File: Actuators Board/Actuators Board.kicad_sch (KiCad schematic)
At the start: 73 parts, among them J1 Conn_01x05_Male, J10 Conn_01x02_Male, J2 Solenoid(Sol), J4 Conn_01x03_Male, J5 Conn_01x06_Male, J9 Conn_01x02_Male, Q1 MMDT2222A, Q2 SI2366DS, U1 ESP32-PICO-D4, U2 TPS54233D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

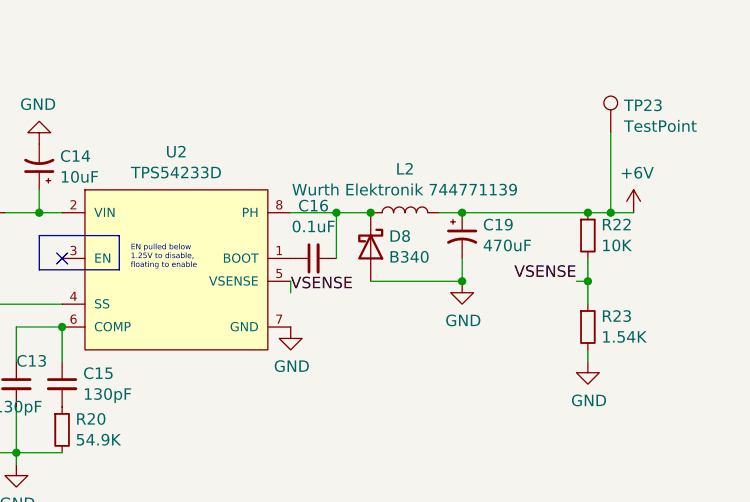
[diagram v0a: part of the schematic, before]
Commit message: Preliminary layout of buck converter components
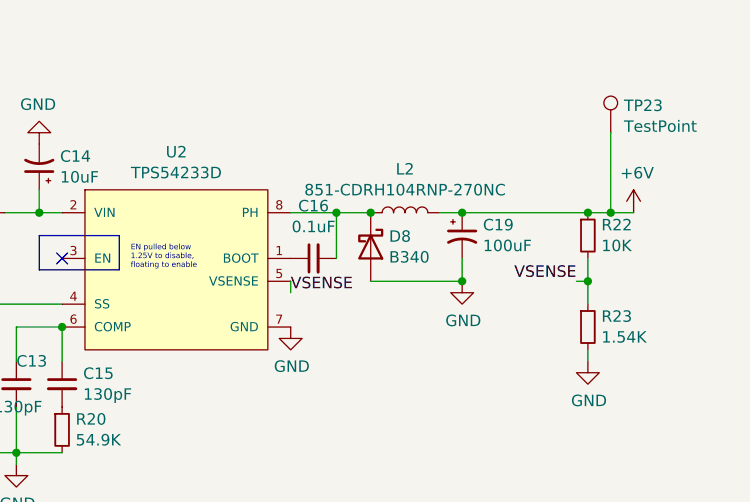
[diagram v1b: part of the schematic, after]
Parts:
- C14: footprint Capacitor_SMD:C_0603_1608Metric -> Capacitor_SMD:CP_Elec_3x5.3
- C19: value 470uF -> 100uF; footprint Capacitor_SMD:CP_Elec_6.3x7.7 -> Capacitor_SMD:CP_Elec_5x5.9
- L2: value Wurth Elektronik 744771139 -> 851-CDRH104RNP-270NC; footprint Inductor_SMD:L_12x12mm_H6mm -> Inductor_SMD:L_10.4x10.4_H4.8
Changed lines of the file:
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@@
     (in_bom yes) (on_board yes)
     (property "Reference" "L2" (id 0) (at 248.92 29.464 90))
-    (property "Value" "Wurth Elektronik 744771139 " (id 1) (at 248.92 31.7754 90))
-    (property "Footprint" "Inductor_SMD:L_12x12mm_H6mm" (id 2) (at 248.92 34.29 0)
+    (property "Value" "851-CDRH104RNP-270NC" (id 1) (at 248.92 31.7754 90))
+    (property "Footprint" "Inductor_SMD:L_10.4x10.4_H4.8" (id 2) (at 248.92 34.29 0)
       (effects (font (size 1.27 1.27)) hide)
     )
@@
     (pin "2")
   )
-  (symbol (lib_id "Connector:TestPoint") (at 34.29 74.93 270)
+  (symbol (lib_id "Connector:TestPoint") (at 34.29 74.93 270) (unit 1)
     (in_bom yes) (on_board yes)
     (property "Reference" "TP4" (id 0) (at 39.0652 73.7616 90)
@@
     (pin "1")
   )
-  (symbol (lib_id "Connector:TestPoint") (at 34.29 72.39 270)
+  (symbol (lib_id "Connector:TestPoint") (at 34.29 72.39 270) (unit 1)
     (in_bom yes) (on_board yes)
     (property "Reference" "TP3" (id 0) (at 39.0652 71.2216 90)
@@
     (pin "1")
   )
-  (symbol (lib_id "Connector:TestPoint") (at 34.29 69.85 270)
+  (symbol (lib_id "Connector:TestPoint") (at 34.29 69.85 270) (unit 1)
     (in_bom yes) (on_board yes)
     (property "Reference" "TP2" (id 0) (at 39.0652 68.6816 90)
@@
     (pin "1")
   )
-  (symbol (lib_id "Connector:TestPoint") (at 34.29 67.31 270)
+  (symbol (lib_id "Connector:TestPoint") (at 34.29 67.31 270) (unit 1)
     (in_bom yes) (on_board yes)
     (property "Reference" "TP1" (id 0) (at 39.0652 66.1416 90)
@@
       (effects (font (size 1.27 1.27)) (justify left))
     )
-    (property "Value" "470uF" (id 1) (at 257.5814 37.973 0)
-      (effects (font (size 1.27 1.27)) (justify left))
-    )
-    (property "Footprint" "Capacitor_SMD:CP_Elec_6.3x7.7" (id 2) (at 255.27 36.83 0)
+    (property "Value" "100uF" (id 1) (at 257.5814 37.973 0)
+      (effects (font (size 1.27 1.27)) (justify left))
+    )
+    (property "Footprint" "Capacitor_SMD:CP_Elec_5x5.9" (id 2) (at 255.27 36.83 0)
       (effects (font (size 1.27 1.27)) hide)
     )
@@
       (effects (font (size 1.27 1.27)) (justify right))
     )
-    (property "Footprint" "Capacitor_SMD:C_0603_1608Metric" (id 2) (at 208.28 29.21 0)
+    (property "Footprint" "Capacitor_SMD:CP_Elec_3x5.3" (id 2) (at 208.28 29.21 0)
       (effects (font (size 1.27 1.27)) hide)
     )
@@
     (pin "1")
   )
-  (symbol (lib_id "power:+3.3V") (at 58.42 92.71 270)
+  (symbol (lib_id "power:+3.3V") (at 58.42 92.71 270) (unit 1)
     (in_bom yes) (on_board yes)
     (property "Reference" "#PWR0108" (id 0) (at 54.61 92.71 0)
@@
     (pin "2")
   )
-  (symbol (lib_id "power:+3.3V") (at 97.79 46.99 0)
+  (symbol (lib_id "power:+3.3V") (at 97.79 46.99 0) (unit 1)
     (in_bom yes) (on_board yes)
     (property "Reference" "#PWR0110" (id 0) (at 97.79 50.8 0)
@@
     (pin "1")
   )
-  (symbol (lib_id "Device:C_Small") (at 95.25 49.53 180)
+  (symbol (lib_id "Device:C_Small") (at 95.25 49.53 180) (unit 1)
     (in_bom yes) (on_board yes)
     (property "Reference" "C4" (id 0) (at 92.71 50.8 0)
@@
     (pin "2")
   )
-  (symbol (lib_id "Device:C_Small") (at 100.33 49.53 0)
+  (symbol (lib_id "Device:C_Small") (at 100.33 49.53 0) (unit 1)
     (in_bom yes) (on_board yes)
     (property "Reference" "C5" (id 0) (at 102.6668 48.3616 0)
@@
     (pin "2")
   )
-  (symbol (lib_id "power:GND") (at 97.79 52.07 0)
+  (symbol (lib_id "power:GND") (at 97.79 52.07 0) (unit 1)
     (in_bom yes) (on_board yes)
     (property "Reference" "#PWR0109" (id 0) (at 97.79 58.42 0)
@@
     )
     (path "/00000000-0000-0000-0000-0000619d12be"
-      (reference "C14") (unit 1) (value "10uF") (footprint "Capacitor_SMD:C_0603_1608Metric")
+      (reference "C14") (unit 1) (value "10uF") (footprint "Capacitor_SMD:CP_Elec_3x5.3")
     )
     (path "/00000000-0000-0000-0000-0000619efcd4"
@@
     )
     (path "/00000000-0000-0000-0000-0000619a1e4e"
-      (reference "C19") (unit 1) (value "470uF") (footprint "Capacitor_SMD:CP_Elec_6.3x7.7")
+      (reference "C19") (unit 1) (value "100uF") (footprint "Capacitor_SMD:CP_Elec_5x5.9")
     )
     (path "/00000000-0000-0000-0000-000061aa4813"
@@
     )
     (path "/00000000-0000-0000-0000-00006199cc35"
-      (reference "L2") (unit 1) (value "Wurth Elektronik 744771139 ") (footprint "Inductor_SMD:L_12x12mm_H6mm")
+      (reference "L2") (unit 1) (value "851-CDRH104RNP-270NC") (footprint "Inductor_SMD:L_10.4x10.4_H4.8")
     )
     (path "/00000000-0000-0000-0000-00005e4f19d5"

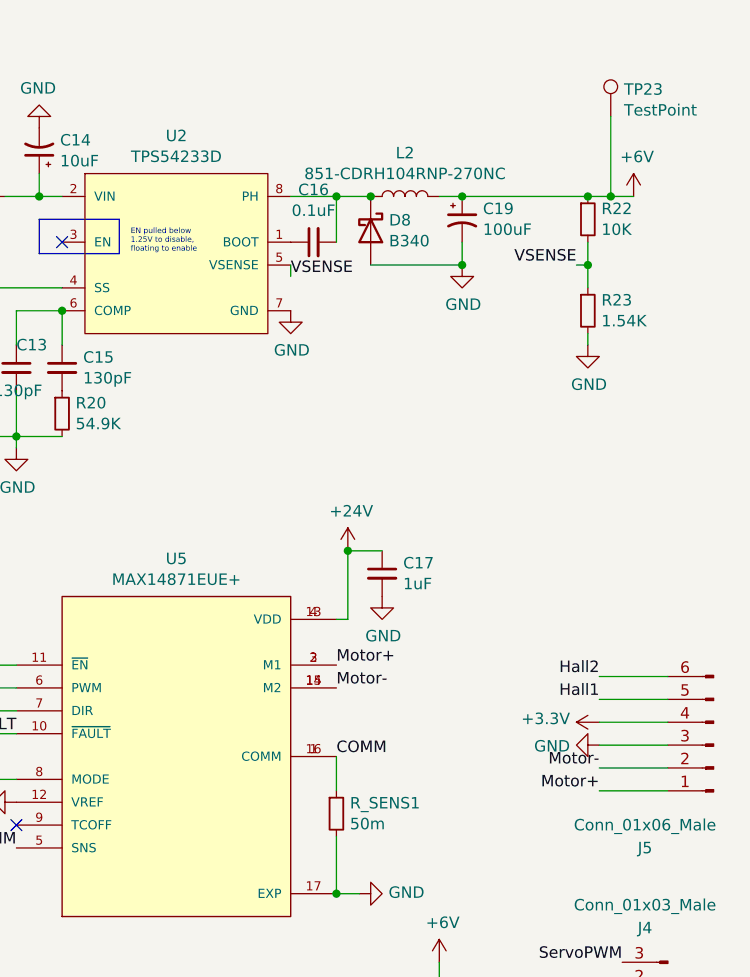
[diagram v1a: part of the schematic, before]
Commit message: changed buck converter inductor & diode to smaller footprints
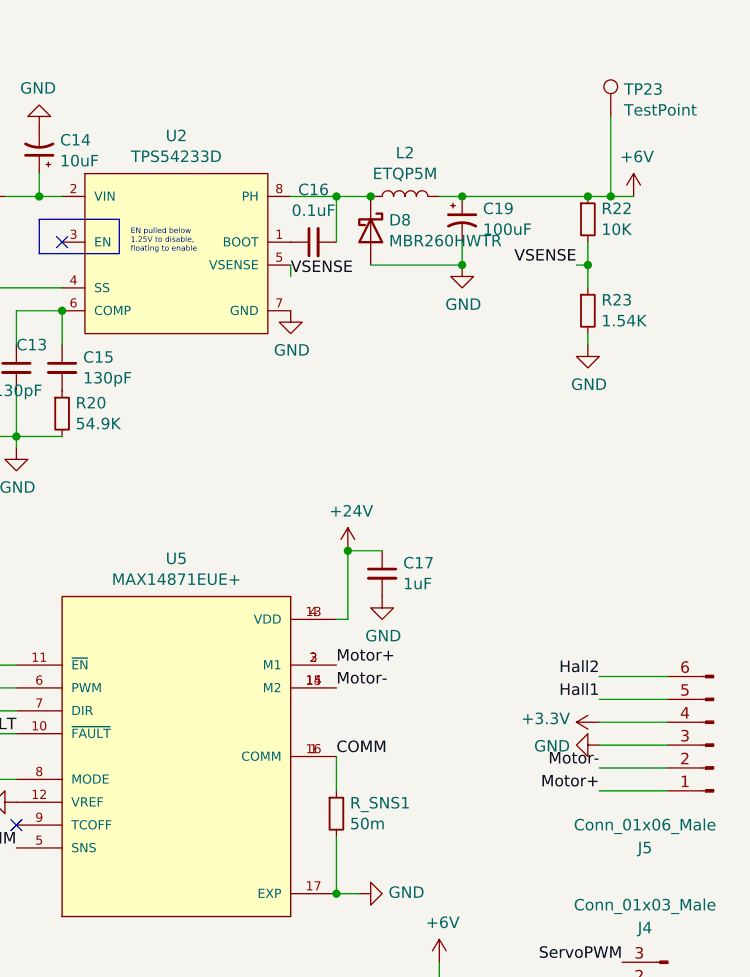
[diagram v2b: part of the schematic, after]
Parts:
- D8: value B340 -> MBR260HWTR; footprint Diode_SMD:D_SMC -> Diode_SMD:D_SOD-123
- L2: value 851-CDRH104RNP-270NC -> ETQP5M; footprint Inductor_SMD:L_10.4x10.4_H4.8 -> iclr:IND_ETQP5M330YFM
- renumbered R_SENS1 to R_SNS1
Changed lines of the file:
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@@
     (in_bom yes) (on_board yes)
     (property "Reference" "L2" (id 0) (at 248.92 29.464 90))
-    (property "Value" "851-CDRH104RNP-270NC" (id 1) (at 248.92 31.7754 90))
-    (property "Footprint" "Inductor_SMD:L_10.4x10.4_H4.8" (id 2) (at 248.92 34.29 0)
+    (property "Value" "ETQP5M" (id 1) (at 248.92 31.7754 90))
+    (property "Footprint" "iclr:IND_ETQP5M330YFM" (id 2) (at 248.92 34.29 0)
       (effects (font (size 1.27 1.27)) hide)
     )
@@
       (effects (font (size 1.27 1.27)) (justify left))
     )
-    (property "Value" "B340" (id 1) (at 247.142 39.243 90)
-      (effects (font (size 1.27 1.27)) (justify left))
-    )
-    (property "Footprint" "Diode_SMD:D_SMC" (id 2) (at 240.665 38.1 0)
+    (property "Value" "MBR260HWTR" (id 1) (at 247.142 39.243 90)
+      (effects (font (size 1.27 1.27)) (justify left))
+    )
+    (property "Footprint" "Diode_SMD:D_SOD-123" (id 2) (at 240.665 38.1 0)
       (effects (font (size 1.27 1.27)) hide)
     )
@@
   (symbol (lib_id "Device:R_Small") (at 241.3 102.87 0) (unit 1)
     (in_bom yes) (on_board yes)
-    (property "Reference" "R_SENS1" (id 0) (at 242.7986 101.7016 0)
+    (property "Reference" "R_SNS1" (id 0) (at 242.7986 101.7016 0)
       (effects (font (size 1.27 1.27)) (justify left))
     )
@@
     )
     (path "/00000000-0000-0000-0000-0000619bfc91"
-      (reference "D8") (unit 1) (value "B340") (footprint "Diode_SMD:D_SMC")
+      (reference "D8") (unit 1) (value "MBR260HWTR") (footprint "Diode_SMD:D_SOD-123")
     )
     (path "/00000000-0000-0000-0000-000061be7627"
@@
     )
     (path "/00000000-0000-0000-0000-00006199cc35"
-      (reference "L2") (unit 1) (value "851-CDRH104RNP-270NC") (footprint "Inductor_SMD:L_10.4x10.4_H4.8")
+      (reference "L2") (unit 1) (value "ETQP5M") (footprint "iclr:IND_ETQP5M330YFM")
     )
     (path "/00000000-0000-0000-0000-00005e4f19d5"
@@
     )
     (path "/00000000-0000-0000-0000-000061bfaaf1"
-      (reference "R_SENS1") (unit 1) (value "50m") (footprint "Resistor_SMD:R_0603_1608Metric")
+      (reference "R_SNS1") (unit 1) (value "50m") (footprint "Resistor_SMD:R_0603_1608Metric")
     )
     (path "/00000000-0000-0000-0000-00006199cf60"
